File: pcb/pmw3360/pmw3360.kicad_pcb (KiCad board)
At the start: 2 copper layers, 22 x 30 mm, 20 parts, among them J1 Connector, J2 PinOut, U1 PMW3360DM-T2QU, U2 TCR2EF19,LM(CT, U3 SN74LVC1T45QDCKRQ1, U4 TXB0104RUT

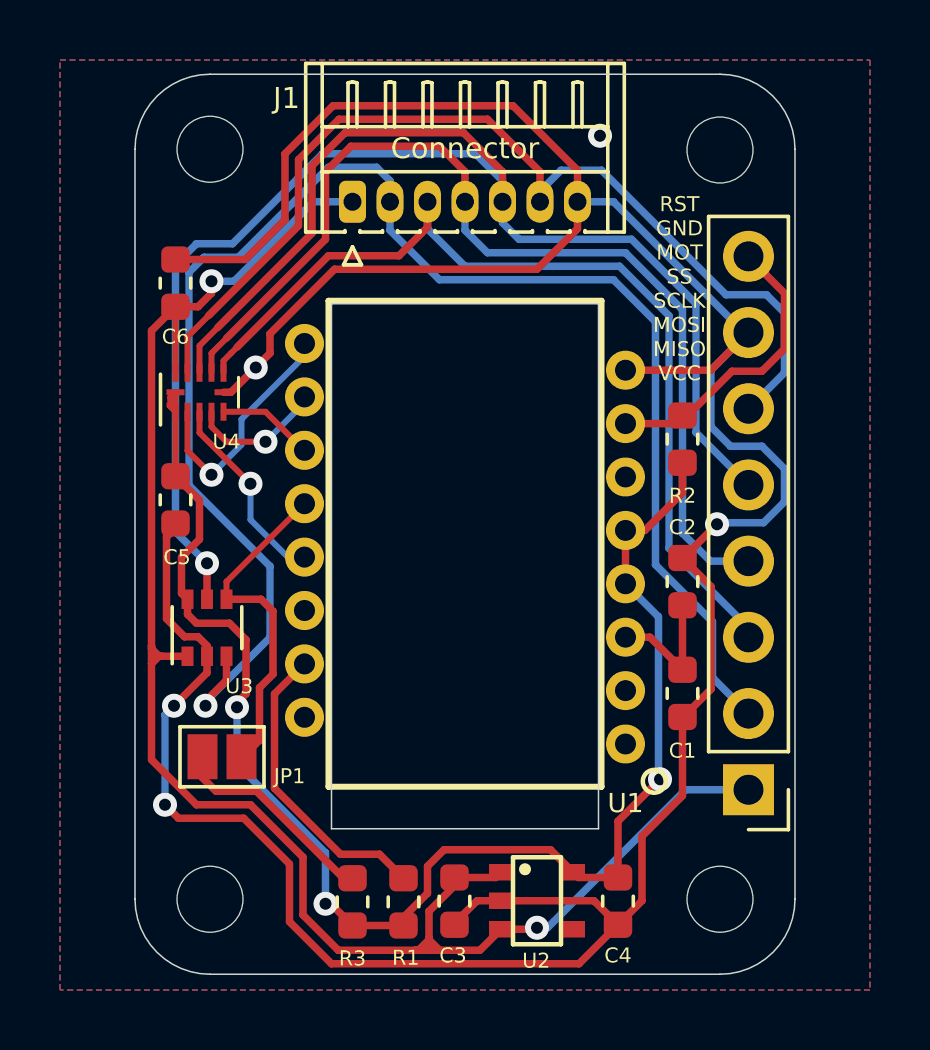
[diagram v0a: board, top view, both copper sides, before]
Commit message: Change VCC, VDD track width
Change VCC, VDD track width
0.25mm -> 0.5mm
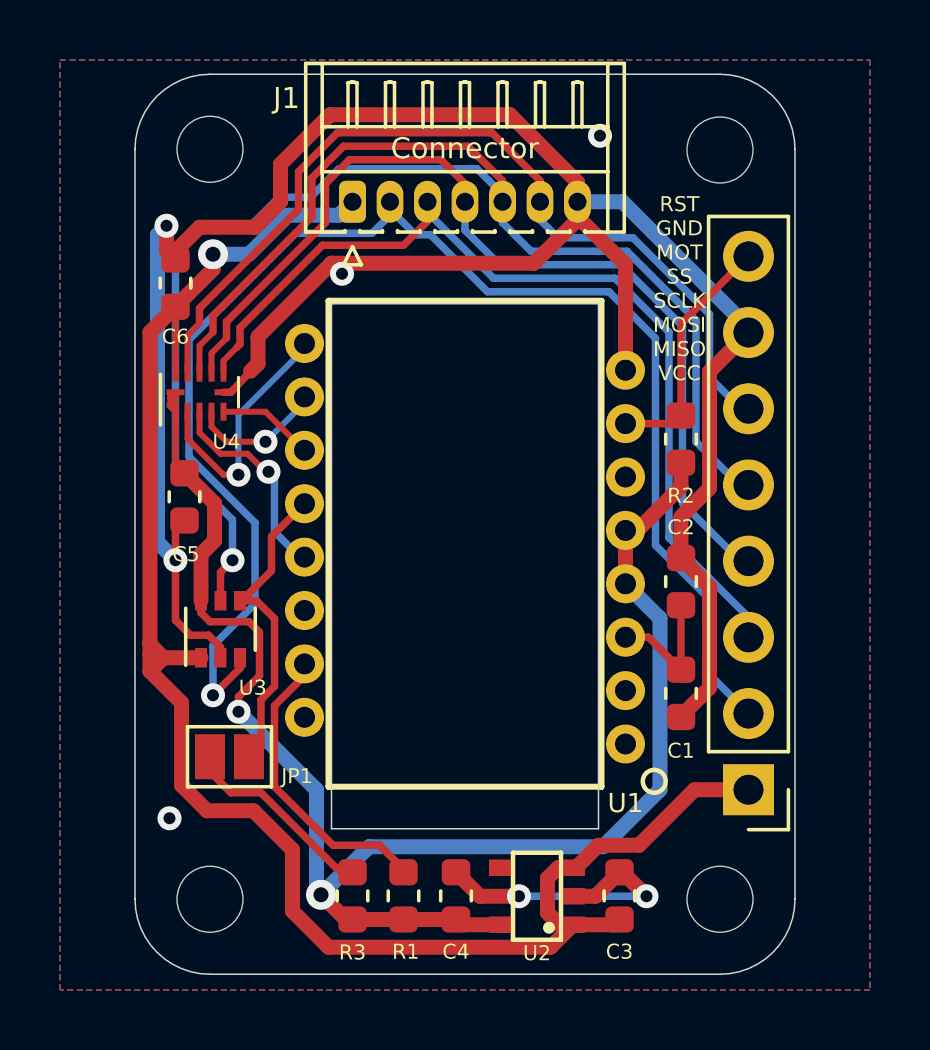
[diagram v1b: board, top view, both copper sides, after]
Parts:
- moved C3 5.50 mm to (111.7, 106.9), turned to 90 degrees
- moved C4 5.40 mm to (106.2, 106.9), turned to 90 degrees
- moved U3 0.45 mm to (98.3, 98.0)
- moved C5 0.32 mm to (97.2, 93.6)
- moved JP1 0.25 mm to (98.7, 102.2)
- moved R1 0.20 mm to (104.5, 106.9)
- moved R3 0.20 mm to (102.8, 106.9)
- moved U2 0.15 mm to (108.9, 106.9), turned to 90 degrees
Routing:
- net GND: track 108.5 -> 91.0 mm, vias 5 -> 7
- net /MISO-H: track 52.8 -> 48.5 mm
- net /MOT-H: track 34.0 -> 30.1 mm
- net VDD: track 49.8 -> 53.1 mm, vias 3 -> 2
- net /SCLK-H: track 34.0 -> 32.2 mm
- net /NRESET: track 9.91 -> 8.20 mm
- net /SS-H: track 56.9 -> 56.1 mm
- net /MISO: track 11.3 -> 10.5 mm
- net VCC: track 58.7 -> 58.2 mm, vias 2 -> 1

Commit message: change route
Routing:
- net /MISO-H: track 48.5 -> 45.4 mm
- net VDD: track 53.1 -> 53.6 mm

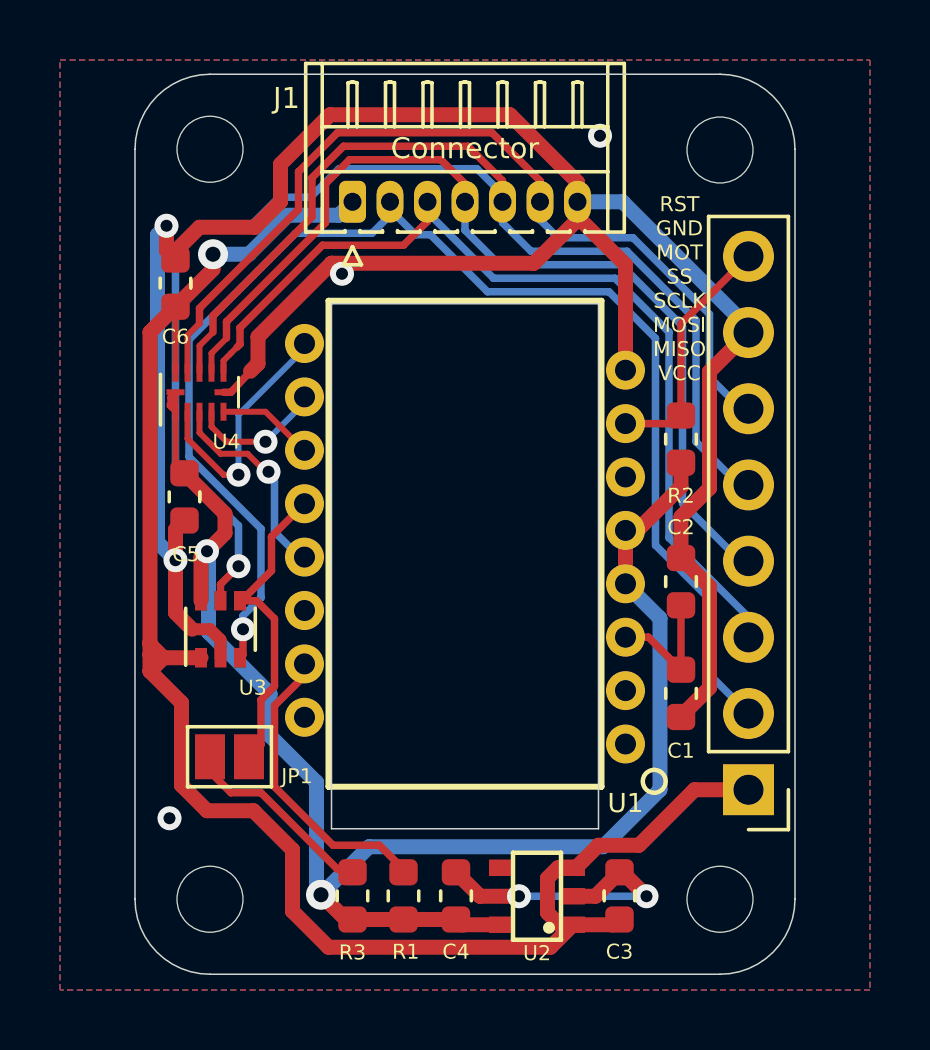
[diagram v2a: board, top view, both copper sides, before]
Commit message: add vias
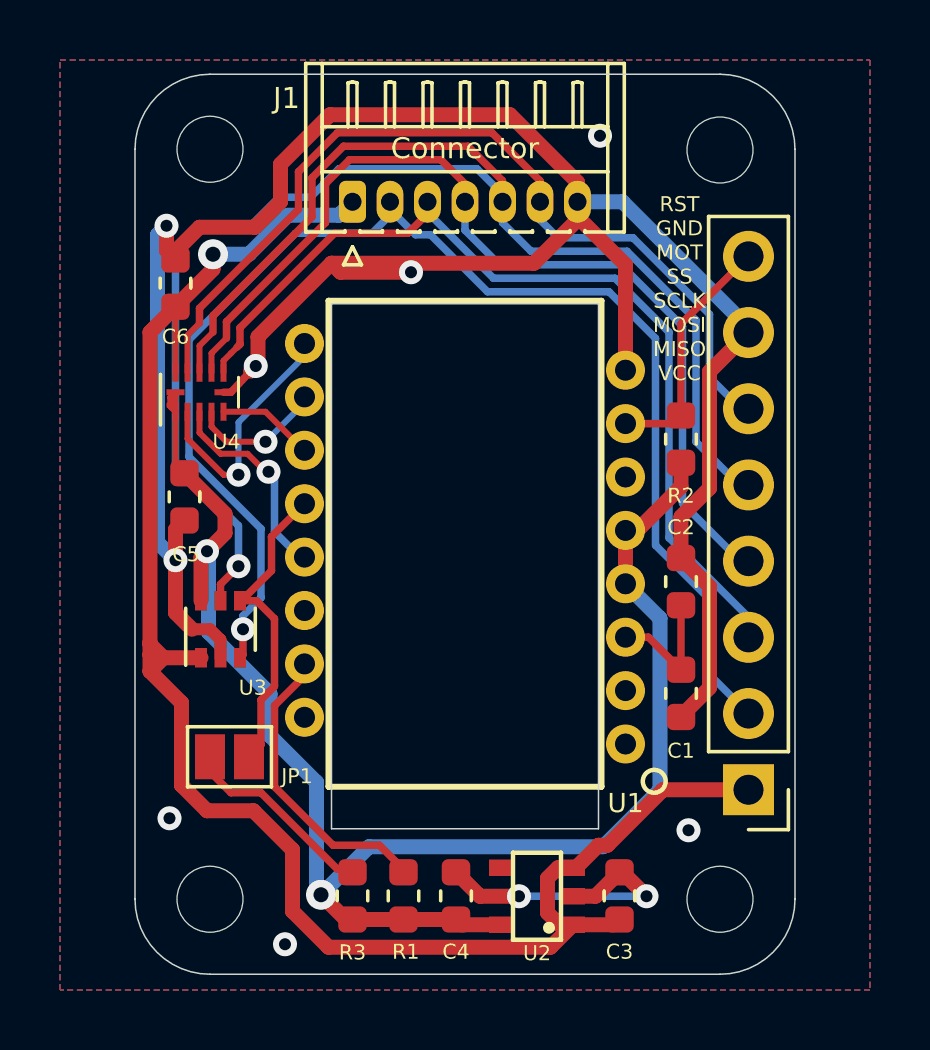
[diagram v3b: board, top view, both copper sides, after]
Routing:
- net GND: track 91.4 -> 93.7 mm, vias 7 -> 10
